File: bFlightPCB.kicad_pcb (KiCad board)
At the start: 2 copper layers, 20 parts, among them SW1 ESC_Pad_D, SW2 ESC_Pad_D, SW3 ESC_Pad_D, SW4 ESC_Pad_D, SW5 ESC_Pad_D, SW6 ESC_Pad_D, U1 WeMos_mini, U2 OLED_I2C_128X64_096IN

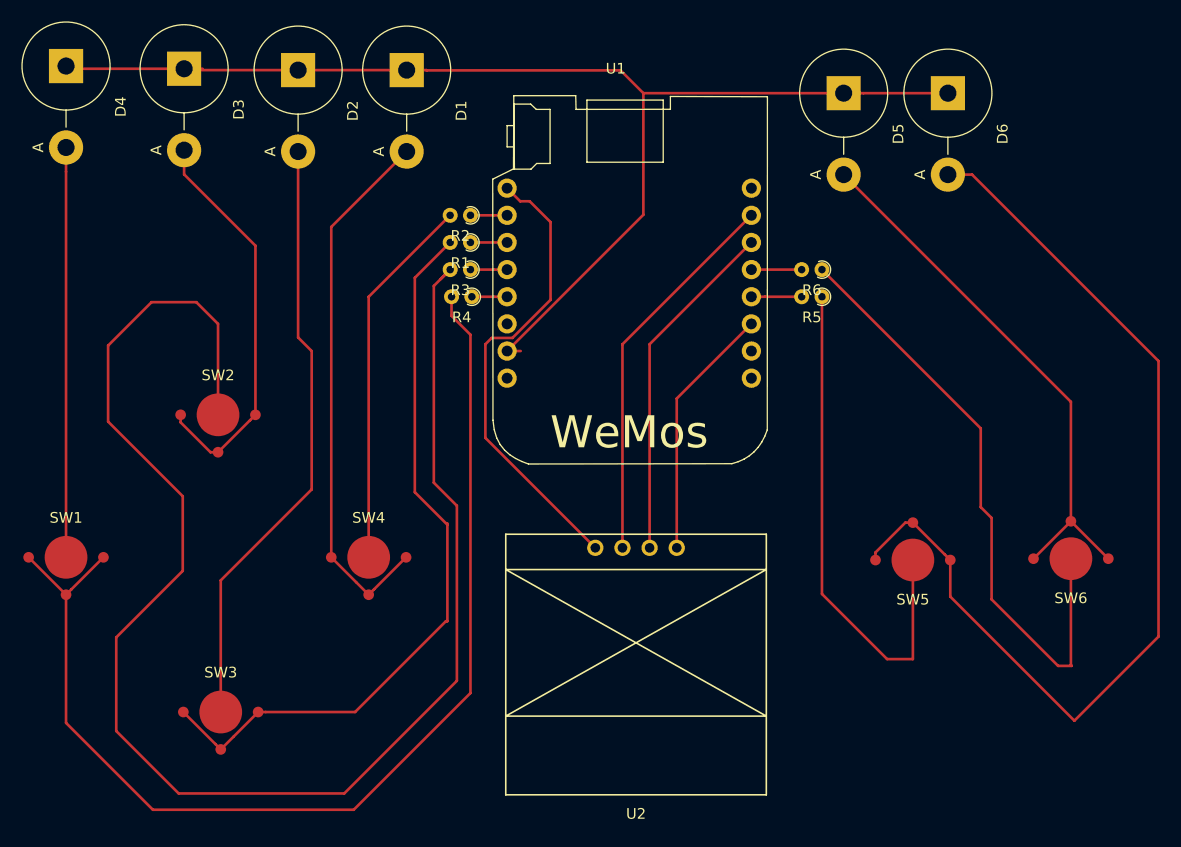
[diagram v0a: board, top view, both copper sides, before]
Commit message: Updated component on PCB to smaller layout
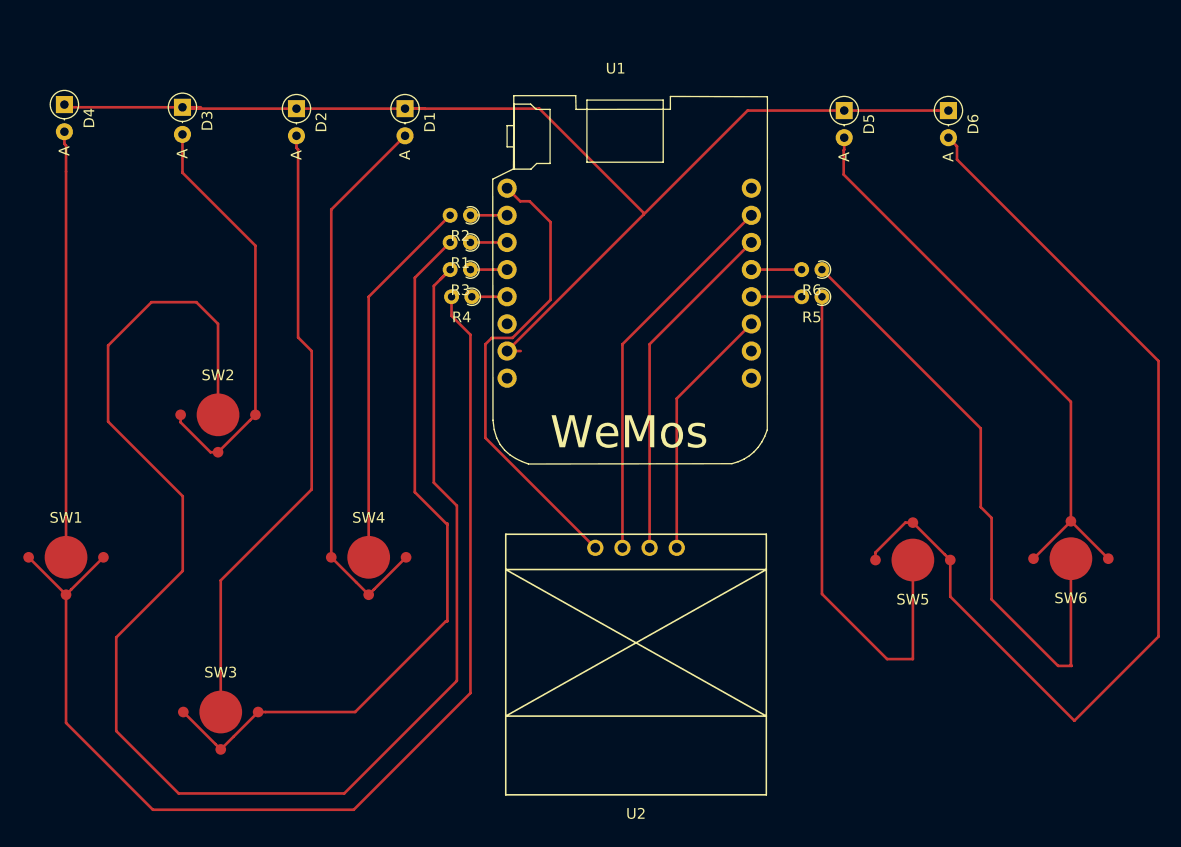
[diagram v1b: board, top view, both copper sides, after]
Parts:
- D1, D2, D3, D4, D5, D6: footprint Diode_THT:D_5KPW_P7.62mm_Vertical_AnodeUp -> Diode_THT:D_DO-35_SOD27_P2.54mm_Vertical_AnodeUp
- moved D1 3.61 mm to (121.5, 25.6)
- moved D2 3.61 mm to (111.4, 25.6)
- moved D3 3.61 mm to (100.7, 25.5)
- moved D4 3.61 mm to (89.6, 25.2)
- moved D5 1.63 mm to (162.6, 25.8)
- moved D6 1.63 mm to (172.4, 25.8)
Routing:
- net Net-(D5-Pad2): track 51.1 -> 54.6 mm
- net Net-(D6-Pad2): track 94.0 -> 96.1 mm
- net Net-(D1-Pad1): track 116.5 -> 114.6 mm
- net Net-(D4-Pad2): track 38.4 -> 39.9 mm
- net Net-(D3-Pad2): track 37.8 -> 39.4 mm
- net Net-(D2-Pad2): track 56.5 -> 58.0 mm
- net Net-(D1-Pad2): track 50.8 -> 52.2 mm
